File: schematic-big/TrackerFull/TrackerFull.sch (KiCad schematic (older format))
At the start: 51 parts, among them J1 SIM_Card, J2 Conn_01x05_Male, J7 Screw_Terminal_01x02, J8 USB_B_Micro, Q1 IRLML5203, Q2 IRLML5203, Q3 IRLML0030, U1 U.FL, U2 LIS3DSH, U3 MCP73831-2-OT, U5 LP2985-3.3, U6 ATtiny85-20SU

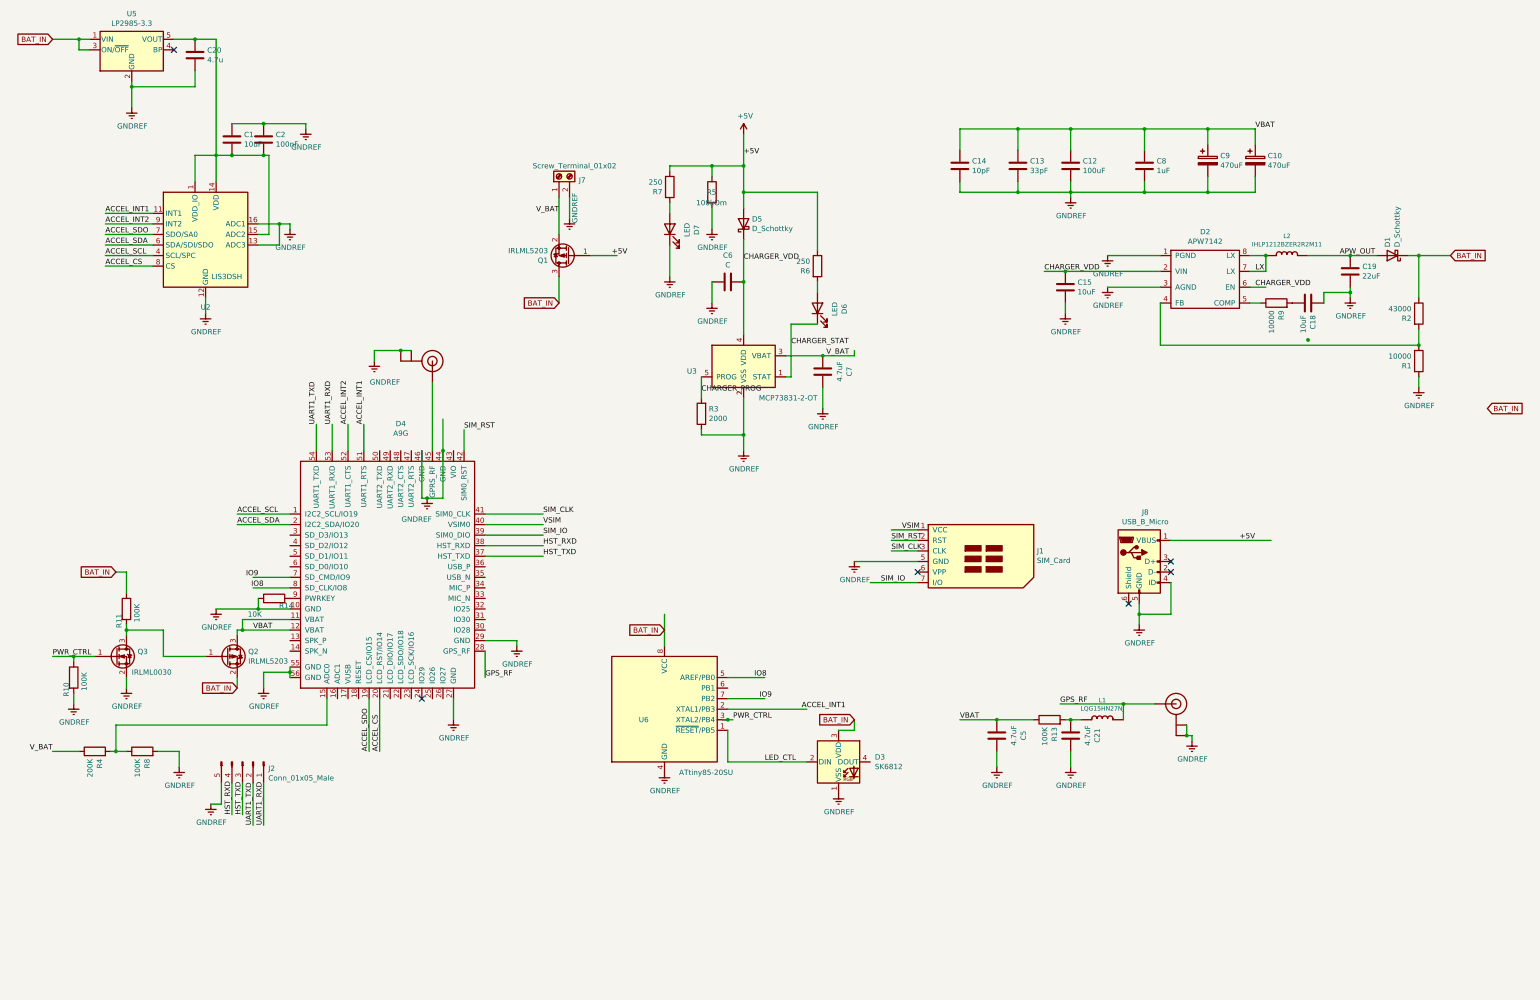
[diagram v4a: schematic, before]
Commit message: schematic update
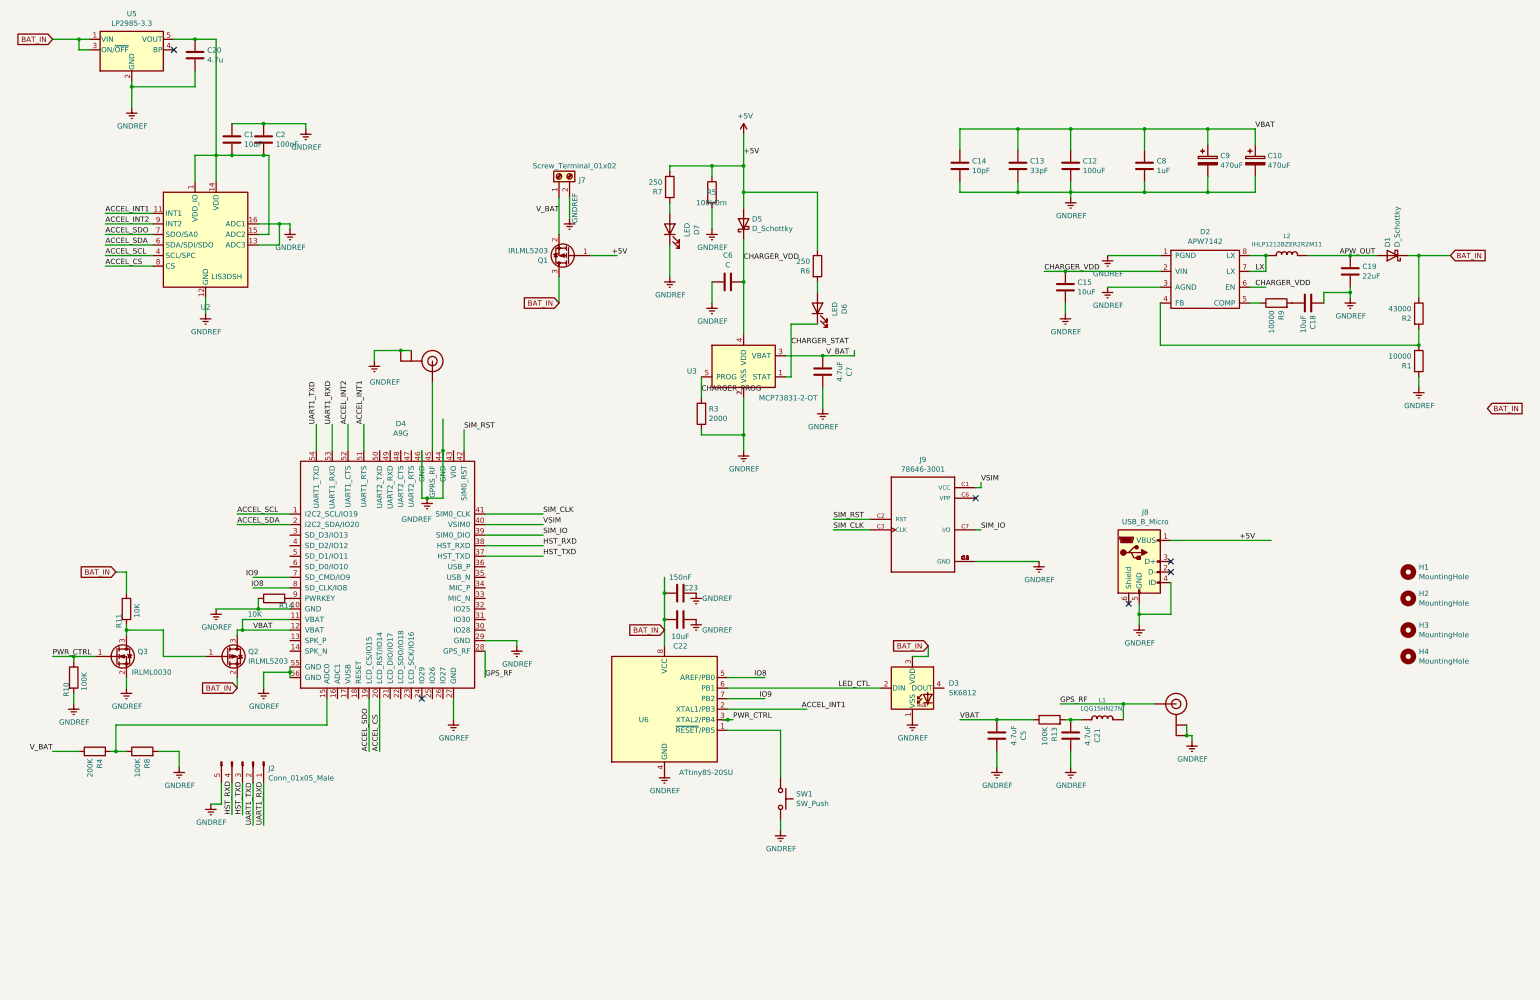
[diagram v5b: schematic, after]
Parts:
- removed J1: SIM_Card, mailboxNotifier:SIM_SOCKET1, symbol Connector:SIM_Card
- added C22: 10uF, Capacitor_SMD:C_0603_1608Metric, symbol Device:C
- added C23: 150nF, Capacitor_SMD:C_0402_1005Metric, symbol Device:C
- added H1, H2, H3, H4: MountingHole, MountingHole:MountingHole_2.2mm_M2, symbol Mechanical:MountingHole
- added J9: 78646-3001, imported:MOLEX_78646-3001, symbol 78646-3001:78646-3001
- added SW1: SW_Push, symbol Switch:SW_Push
- C13: footprint Capacitor_SMD:C_1206_3216Metric_Pad1.42x1.75mm_HandSolder -> Capacitor_SMD:C_0201_0603Metric
- C14: footprint Capacitor_SMD:C_1206_3216Metric_Pad1.42x1.75mm_HandSolder -> Capacitor_SMD:C_0402_1005Metric
- C2: footprint Capacitor_SMD:C_0603_1608Metric -> Capacitor_SMD:C_0402_1005Metric
- C20, C21, C5, C6, C7, C8: footprint Capacitor_SMD:C_1206_3216Metric_Pad1.42x1.75mm_HandSolder -> Capacitor_SMD:C_0603_1608Metric
- R11: value 100K -> 10K
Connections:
- wire segments 212 -> 217
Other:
- moved on the sheet: D3

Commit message: Last schematic
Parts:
- removed J2: Conn_01x05_Male, Connector_PinHeader_2.54mm:PinHeader_1x05_P2.54mm_Vertical, symbol Connector:Conn_01x05_Male
- removed J8: USB_B_Micro, Connector_USB:USB_Micro-B_Molex-105017-0001, symbol Connector:USB_B_Micro
- added J1, J5: Conn_01x02_Male, Connector_PinHeader_2.54mm:PinHeader_1x02_P2.54mm_Vertical, symbol Connector:Conn_01x02_Male
- added J3: AVR-ISP-6, Connector_PinHeader_2.54mm:PinHeader_2x03_P2.54mm_Vertical, symbol Connector:AVR-ISP-6
- added J6: Screw_Terminal_01x02, Connector_JST:JST_PH_B2B-PH-K_1x02_P2.00mm_Vertical, symbol Connector:Screw_Terminal_01x02
- added R11, R12, R13: 4700, Resistor_SMD:R_0603_1608Metric, symbol Device:R
- added R14: 470, Resistor_SMD:R_0603_1608Metric, symbol Device:R
- added R5, R6: 10K, Resistor_SMD:R_0603_1608Metric, symbol Device:R
- C15: renamed from C9; footprint Capacitor_THT:CP_Radial_D8.0mm_P3.50mm -> Capacitor_SMD:CP_Elec_8x10.5
- C16: renamed from C10; footprint Capacitor_THT:CP_Radial_D8.0mm_P3.50mm -> Capacitor_SMD:CP_Elec_8x10.5
- J2: renamed from J7; footprint Connector_Wire:SolderWirePad_1x02_P5.08mm_Drill1.5mm -> Connector_JST:JST_PH_B2B-PH-K_1x02_P2.00mm_Vertical
- SW1: footprint (none) -> Button_Switch_SMD:SW_Push_1P1T_NO_6x6mm_H9.5mm
- renumbered C20 to C1, C13 to C10, C15 to C11, C21 to C13, C8 to C14, C18 to C17, C19 to C18, C1 to C2, C2 to C3, C23 to C4, C22 to C5, C14 to C8, C5 to C9, D4 to D1, D7 to D2, D5 to D3, D6 to D4, D3 to D5, D2 to D6, D1 to D7, J9 to J4, Q3 to Q1, Q1 to Q3, R10 to R1, R5 to R10, R6 to R15, R13 to R16, R9 to R17, R2 to R18, R1 to R19, R4 to R2, R11 to R3, R8 to R4, R14 to R7, R7 to R8, R3 to R9, U5 to U1, U6 to U3, U3 to U4, U1 to U5
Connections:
- net labels added: 3.3v, AVR_MISO, AVR_MOSI_SDA, AVR_RST, AVR_SCK, ICSP_MISO, ICSP_MOSI, ICSP_RST, ICSP_SCK
- net labels removed: IO8, IO9
- wire segments 217 -> 230
- no-connect marks 6 -> 3
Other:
- moved on the sheet: D5

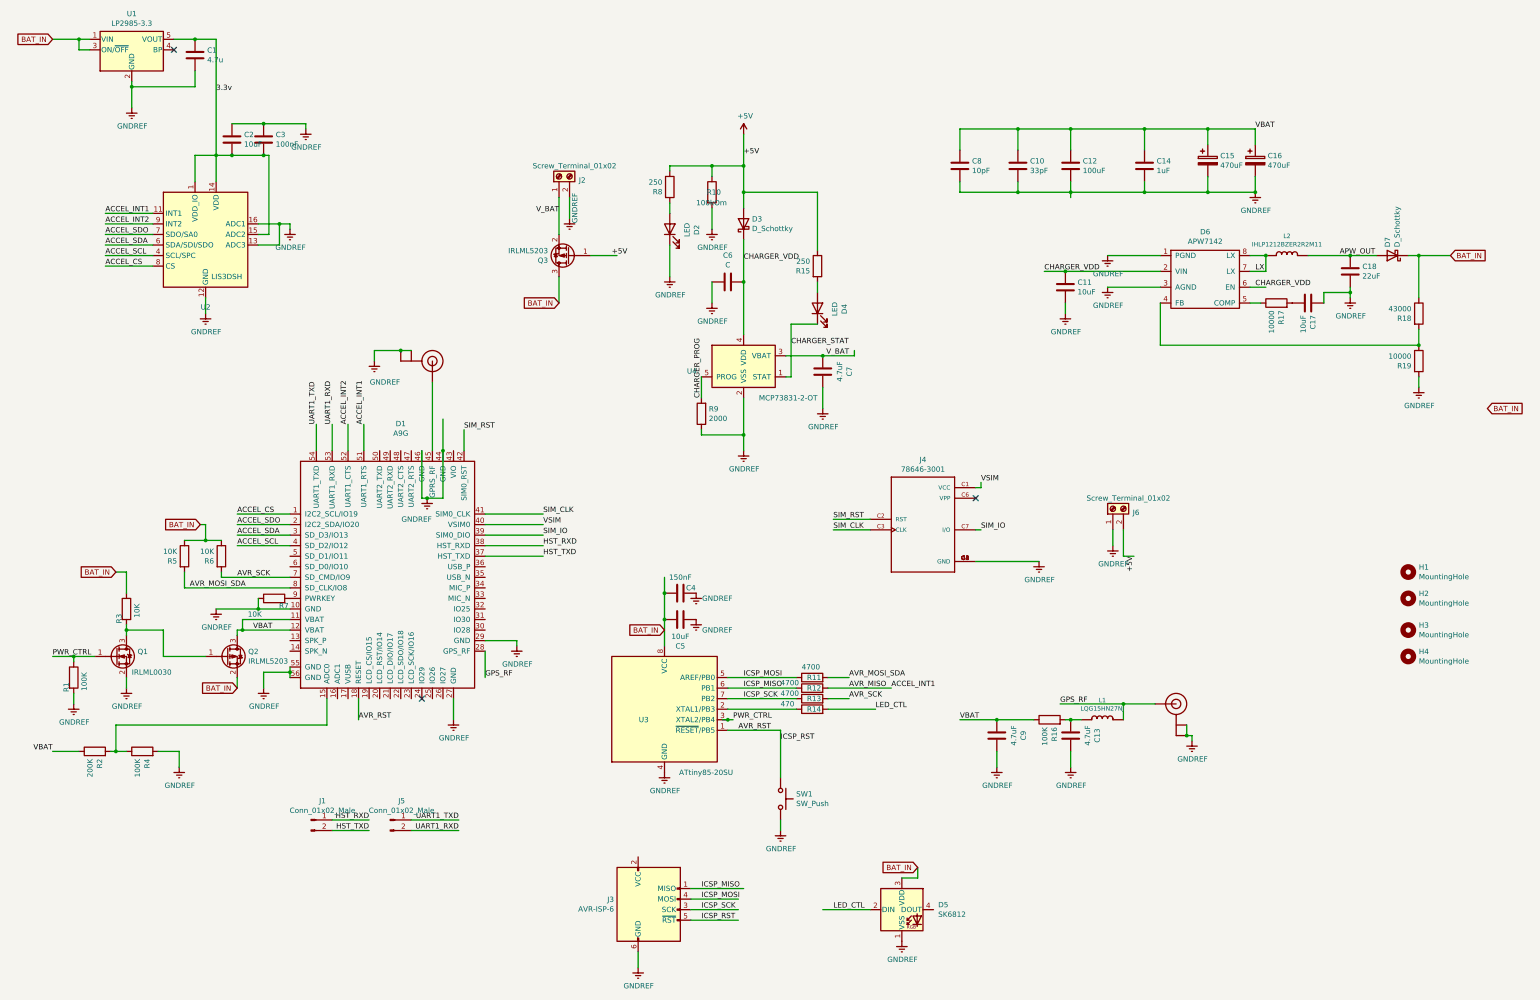
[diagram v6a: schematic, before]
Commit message: schematic update
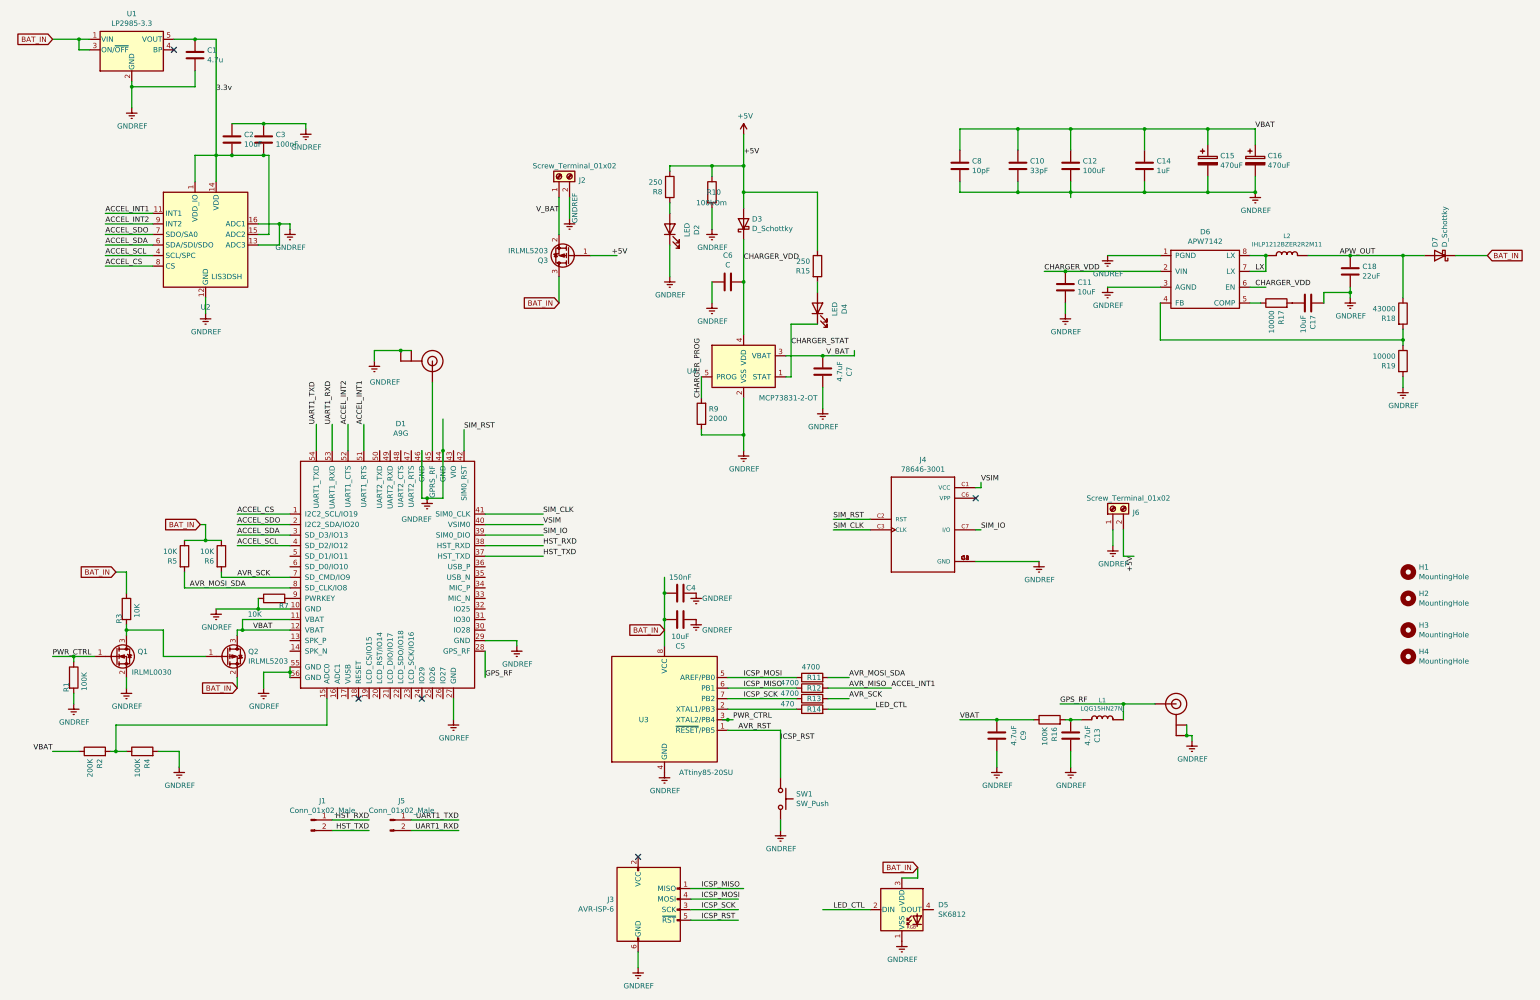
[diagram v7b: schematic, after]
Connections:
- no-connect marks 3 -> 5
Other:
- moved on the sheet: D7, R18, R19
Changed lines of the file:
@@
 Wire Wire Line
 	7050 2450 7450 2450
-Text GLabel 14800 4750 2    50   Input ~ 0
-BAT_IN
 Text Label 5850 5850 0    50   ~ 0
 VSIM
@@
 L Device:D_Schottky D7
 U 1 1 5F5BE753
-P 13900 3300
-F 0 "D7" V 13946 3221 50  0000 R CNN
-F 1 "D_Schottky" V 13855 3221 50  0000 R CNN
-F 2 "Diode_SMD:D_SMA" H 13900 3300 50  0001 C CNN
-F 3 "~" H 13900 3300 50  0001 C CNN
-	1    13900 3300
+P 14350 3300
+F 0 "D7" V 14396 3221 50  0000 R CNN
+F 1 "D_Schottky" V 14305 3221 50  0000 R CNN
+F 2 "Diode_SMD:D_SMA" H 14350 3300 50  0001 C CNN
+F 3 "~" H 14350 3300 50  0001 C CNN
+	1    14350 3300
 	-1   0    0    1
 $EndComp
@@
 L Device:R R19
 U 1 1 5F8B8213
-P 14150 4300
-F 0 "R19" H 14080 4254 50  0000 R CNN
-F 1 "10000" H 14080 4345 50  0000 R CNN
-F 2 "Resistor_SMD:R_0603_1608Metric" H 14080 4391 50  0001 R CNN
-F 3 "~" H 14150 4300 50  0001 C CNN
-	1    14150 4300
+P 14000 4300
+F 0 "R19" H 13930 4254 50  0000 R CNN
+F 1 "10000" H 13930 4345 50  0000 R CNN
+F 2 "Resistor_SMD:R_0603_1608Metric" H 13930 4391 50  0001 R CNN
+F 3 "~" H 14000 4300 50  0001 C CNN
+	1    14000 4300
 	1    0    0    -1
 $EndComp
@@
 L Device:R R18
 U 1 1 5F8B8DB4
-P 14150 3850
-F 0 "R18" H 14080 3804 50  0000 R CNN
-F 1 "43000" H 14080 3895 50  0000 R CNN
-F 2 "Resistor_SMD:R_0603_1608Metric" H 14080 3941 50  0001 R CNN
-F 3 "~" H 14150 3850 50  0001 C CNN
-	1    14150 3850
+P 14000 3850
+F 0 "R18" H 13930 3804 50  0000 R CNN
+F 1 "43000" H 13930 3895 50  0000 R CNN
+F 2 "Resistor_SMD:R_0603_1608Metric" H 13930 3941 50  0001 R CNN
+F 3 "~" H 14000 3850 50  0001 C CNN
+	1    14000 3850
 	1    0    0    -1
 $EndComp
@@
 L power:GNDREF #PWR038
 U 1 1 5F98AFC6
-P 14150 4550
+P 14000 4550
 AR Path="/5F98AFC6" Ref="#PWR038"  Part="1"
 AR Path="/5F3BC941/5F98AFC6" Ref="#PWR?"  Part="1"
-F 0 "#PWR038" H 14150 4300 50  0001 C CNN
-F 1 "GNDREF" H 14155 4377 50  0000 C CNN
-F 2 "" H 14150 4550 50  0001 C CNN
-F 3 "" H 14150 4550 50  0001 C CNN
-	1    14150 4550
-	1    0    0    -1
-$EndComp
-Wire Wire Line
-	14150 4550 14150 4450
+F 0 "#PWR038" H 14000 4300 50  0001 C CNN
+F 1 "GNDREF" H 14005 4377 50  0000 C CNN
+F 2 "" H 14000 4550 50  0001 C CNN
+F 3 "" H 14000 4550 50  0001 C CNN
+	1    14000 4550
+	1    0    0    -1
+$EndComp
+Wire Wire Line
+	14000 4550 14000 4450
 $Comp
 L Device:C C18
@@
 	1    0    0    -1
 $EndComp
-Connection ~ 13500 3300
-Wire Wire Line
-	13500 3300 13750 3300
-Wire Wire Line
-	14050 3300 14150 3300
 $Comp
 L power:GNDREF #PWR037
@@
 	13500 3700 13500 3650
 Wire Wire Line
-	14150 3300 14150 3700
-Connection ~ 14150 3300
-Wire Wire Line
-	14150 3300 14450 3300
+	14000 3300 14000 3700
 $Comp
 L Device:C C11
@@
 	10800 3750 10800 3850
 Connection ~ 12700 3300
-Text GLabel 14450 3300 2    50   Input ~ 0
+Text GLabel 14800 3300 2    50   Input ~ 0
 BAT_IN
 $Comp
@@
 $EndComp
 Wire Wire Line
-	14150 4000 14150 4150
-Wire Wire Line
 	12550 3750 12650 3750
 Wire Wire Line
@@
 	13500 3650 13500 3600
 Wire Wire Line
-	11700 3750 11700 4150
-Wire Wire Line
-	11700 4150 14150 4150
-Connection ~ 14150 4150
+	11700 3750 11700 4100
 $Comp
 L Transistor_FET:IRLML5203 Q2
@@
 Text Label 7700 7800 0    50   ~ 0
 AVR_RST
-Text Label 4100 7700 0    50   ~ 0
-AVR_RST
-Wire Wire Line
-	4100 7500 4100 7700
 $Comp
 L Device:R R11
@@
 Wire Wire Line
 	4600 8750 5050 8750
+NoConn ~ 6750 9000
+Wire Wire Line
+	13500 3300 14000 3300
+Connection ~ 13500 3300
+Wire Wire Line
+	14000 3300 14200 3300
+Connection ~ 14000 3300
+Wire Wire Line
+	14500 3300 14800 3300
+Wire Wire Line
+	14000 4000 14000 4100
+Wire Wire Line
+	14000 4100 11700 4100
+Connection ~ 14000 4100
+Wire Wire Line
+	14000 4100 14000 4150
+NoConn ~ 4100 7500
 $EndSCHEMATC

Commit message: latest version. Doesnt work :)
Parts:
- removed H2: MountingHole, MountingHole:MountingHole_2.2mm_M2, symbol Mechanical:MountingHole
- removed J3: AVR-ISP-6, Connector_PinHeader_2.54mm:PinHeader_2x03_P2.54mm_Vertical, symbol Connector:AVR-ISP-6
- removed R11, R12, R13: 4700, Resistor_SMD:R_0603_1608Metric, symbol Device:R
- added R?: 10K, Resistor_SMD:R_0603_1608Metric, symbol Device:R
- U3: value ATtiny85-20SU -> ATtiny85-20PU; footprint Package_SO:SOIJ-8_5.3x5.3mm_P1.27mm -> Package_DIP:DIP-8_W7.62mm
- renumbered J5 to J2, J2 to J3, J6 to J5, R14 to R11, R15 to R12, R16 to R13, R17 to R14, R18 to R15, R19 to R16
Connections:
- net labels removed: ICSP_MISO, ICSP_MOSI, ICSP_SCK
- wire segments 230 -> 223
- no-connect marks 5 -> 4
